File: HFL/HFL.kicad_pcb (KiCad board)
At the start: 2 copper layers, 62.6 x 37.6 mm, 28 parts, among them J1 Conn_01x06_Male, J2 FOUT, J3 PWR, J4 SHTDN, J5 HFR, K1 G5V-1, K2 G5V-1, K3 G5V-1, K4 G5V-1, K5 OMRON-G2R-24

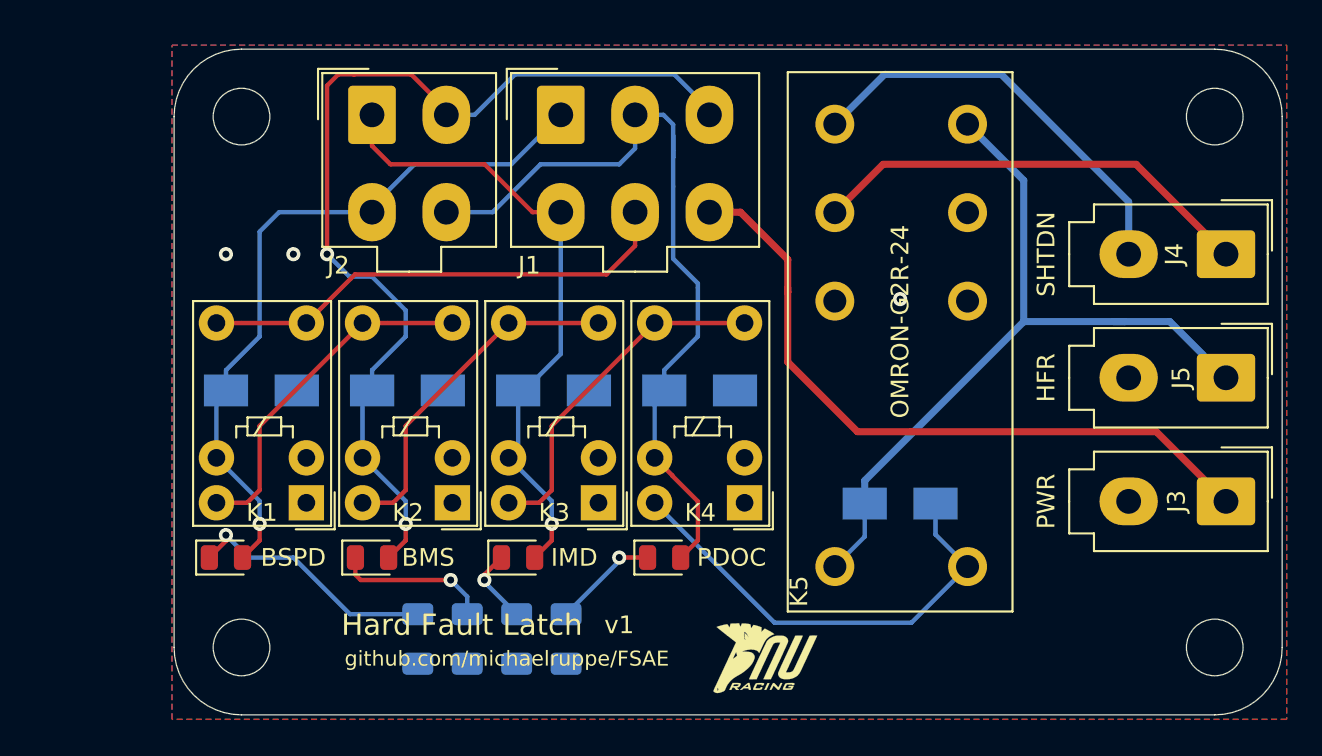
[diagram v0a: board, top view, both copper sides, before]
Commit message: Update HFL PCB - preliminary component placement
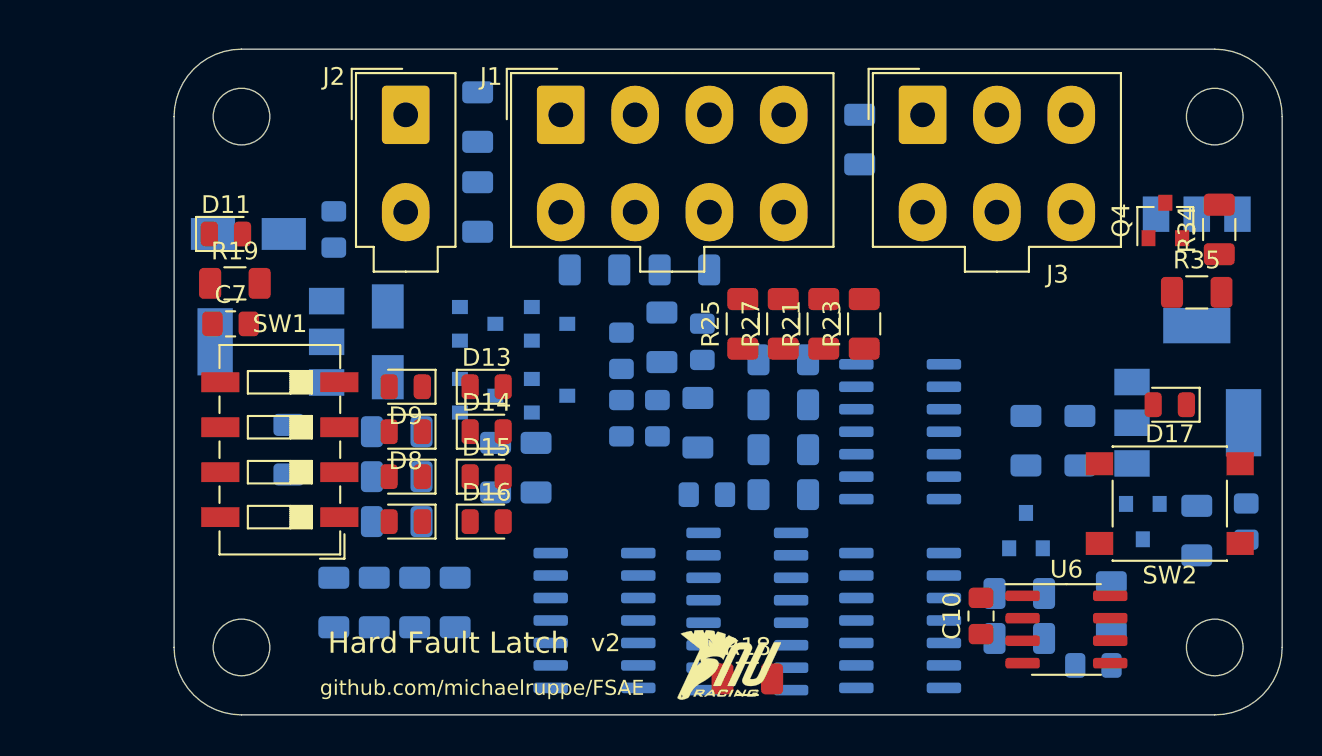
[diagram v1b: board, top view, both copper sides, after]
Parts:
- removed J4: SHTDN, Connector_Molex:Molex_Mini-Fit_Jr_5566-02A_2x01_P4.20mm_Vertical
- removed J5: HFR, Connector_Molex:Molex_Mini-Fit_Jr_5566-02A_2x01_P4.20mm_Vertical
- removed K1, K2, K3, K4: G5V-1, Relay_THT:Relay_SPDT_Omron_G5V-1
- removed K5: OMRON-G2R-24, HFL:OMRON-G2R-24
- added C1: 10n, Capacitor_SMD:C_0805_2012Metric_Pad1.15x1.40mm_HandSolder, B.Cu at (103.5, 66.6)
- added C10: 1u, Capacitor_SMD:C_0805_2012Metric_Pad1.15x1.40mm_HandSolder, F.Cu at (121.8, 77.8)
- added C2: 10n, Capacitor_SMD:C_0805_2012Metric_Pad1.15x1.40mm_HandSolder, B.Cu at (101.5, 66.6)
- added C3: 10n, Capacitor_SMD:C_0805_2012Metric_Pad1.15x1.40mm_HandSolder, B.Cu at (106.1, 62.3)
- added C4: 10n, Capacitor_SMD:C_0805_2012Metric_Pad1.15x1.40mm_HandSolder, B.Cu at (101.5, 62.8)
- added C5: 100n, Capacitor_SMD:C_0805_2012Metric_Pad1.15x1.40mm_HandSolder, B.Cu at (106.3, 70.9)
- added C6: 1u, Capacitor_SMD:C_0805_2012Metric_Pad1.15x1.40mm_HandSolder, B.Cu at (85.2, 55.9)
- added C7: 1u, Capacitor_SMD:C_0805_2012Metric_Pad1.15x1.40mm_HandSolder, F.Cu at (79.4, 61.2)
- added C8: 1u, Capacitor_SMD:C_0805_2012Metric_Pad1.15x1.40mm_HandSolder, B.Cu at (136.8, 72.4)
- added C9: 10n, Capacitor_SMD:C_0805_2012Metric_Pad1.15x1.40mm_HandSolder, B.Cu at (128.2, 80.5)
- added D10: D, Diode_SMD:D_SMA, B.Cu at (88.3, 62.3)
- added D11: PWR, LED_SMD:LED_0805_2012Metric, F.Cu at (79.1, 56.2)
- added D12: BZX84Cxx, Diode_SMD:D_SOT-23_ANK, B.Cu at (130.9, 72.4)
- added D13: IMD-OK, LED_SMD:LED_0805_2012Metric, F.Cu at (93.9, 64.8)
- added D14: BSPD-OK, LED_SMD:LED_0805_2012Metric, F.Cu at (93.9, 67.3)
- added D15: BMS-OK, LED_SMD:LED_0805_2012Metric, F.Cu at (93.9, 69.9)
- added D16: PDOC-OK, LED_SMD:LED_0805_2012Metric, F.Cu at (93.9, 72.4)
- added D17: FAULT, LED_SMD:LED_0805_2012Metric, F.Cu at (132.5, 65.8)
- added Q1: 2N7002, Package_TO_SOT_SMD:SOT-23, B.Cu at (124.3, 72.9)
- added Q2: MCT06P10-TP, Package_TO_SOT_SMD:SOT-223-3_TabPin2, B.Cu at (133.5, 66.8)
- added Q3: MCT06P10-TP, Package_TO_SOT_SMD:SOT-223-3_TabPin2, B.Cu at (134.0, 58.2)
- added Q4: 2N7002, Package_TO_SOT_SMD:SOT-23, F.Cu at (132.2, 55.4)
- added R10: 10k, Resistor_SMD:R_1206_3216Metric, B.Cu at (87.5, 77.0)
- added R11: 10k, Resistor_SMD:R_1206_3216Metric, B.Cu at (89.8, 77.0)
- added R12: 10k, Resistor_SMD:R_1206_3216Metric, B.Cu at (92.1, 77.0)
- added R13: 330, Resistor_SMD:R_1206_3216Metric, B.Cu at (88.8, 72.4)
- added R14: 330, Resistor_SMD:R_1206_3216Metric, B.Cu at (88.8, 69.9)
- added R15: 330, Resistor_SMD:R_1206_3216Metric, B.Cu at (88.8, 67.3)
- added R16: 330, Resistor_SMD:R_1206_3216Metric, B.Cu at (82.7, 68.4)
- added R17: 1k, Resistor_SMD:R_1206_3216Metric, B.Cu at (114.9, 50.8)
- added R18: 100k, Resistor_SMD:R_1206_3216Metric, F.Cu at (108.6, 81.3)
- added R19: 3k3, Resistor_SMD:R_1206_3216Metric, F.Cu at (79.6, 59.0)
- added R20: 1k, Resistor_SMD:R_1206_3216Metric, B.Cu at (134.0, 72.9)
- added R21: 1k, Resistor_SMD:R_1206_3216Metric, F.Cu at (112.9, 61.2)
- added R22: 2k7, Resistor_SMD:R_1206_3216Metric, B.Cu at (110.6, 63.3)
- added R23: 1k, Resistor_SMD:R_1206_3216Metric, F.Cu at (115.2, 61.2)
- added R24: 2k7, Resistor_SMD:R_1206_3216Metric, B.Cu at (110.6, 70.9)
- added R25: 1k, Resistor_SMD:R_1206_3216Metric, F.Cu at (108.3, 61.2)
- added R26: 2k7, Resistor_SMD:R_1206_3216Metric, B.Cu at (110.6, 68.4)
- added R27: 1k, Resistor_SMD:R_1206_3216Metric, F.Cu at (110.6, 61.2)
- added R28: 2k7, Resistor_SMD:R_1206_3216Metric, B.Cu at (110.6, 65.8)
- added R29: 100k, Resistor_SMD:R_1206_3216Metric, B.Cu at (124.0, 76.5)
- added R30: 100k, Resistor_SMD:R_1206_3216Metric, B.Cu at (124.3, 67.8)
- added R31: 10k, Resistor_SMD:R_1206_3216Metric, B.Cu at (127.4, 67.8)
- added R32: 150k, Resistor_SMD:R_1206_3216Metric, B.Cu at (124.0, 79.0)
- added R33: 100k, Resistor_SMD:R_1206_3216Metric, B.Cu at (129.2, 77.2)
- added R34: 10k, Resistor_SMD:R_1206_3216Metric, F.Cu at (135.3, 55.9)
- added R35: 2k2, Resistor_SMD:R_1206_3216Metric, F.Cu at (134.0, 59.5)
- added R5: 100k, Resistor_SMD:R_1206_3216Metric, B.Cu at (105.8, 66.8)
- added R6: 100k, Resistor_SMD:R_1206_3216Metric, B.Cu at (96.7, 69.4)
- added R7: 100k, Resistor_SMD:R_1206_3216Metric, B.Cu at (94.4, 69.4)
- added R8: 100k, Resistor_SMD:R_1206_3216Metric, B.Cu at (103.8, 62.0)
- added R9: 10k, Resistor_SMD:R_1206_3216Metric, B.Cu at (85.2, 77.0)
- added SW1: BYPASS, Button_Switch_SMD:SW_DIP_SPSTx04_Slide_6.7x11.72mm_W6.73mm_P2.54mm_LowProfile_JPin, F.Cu at (82.2, 68.4)
- added SW2: SW_Push, Button_Switch_SMD:SW_Push_1P1T_NO_6x6mm_H9.5mm, F.Cu at (132.5, 71.4)
- added U1: 74LS32, Package_SO:SOIC-14_3.9x8.7mm_P1.27mm, B.Cu at (100.0, 78.0)
- added U2: 74LS08, Package_SO:SOIC-14_3.9x8.7mm_P1.27mm, B.Cu at (117.2, 78.0)
- added U3: MCP6004, Package_SO:SOIC-14_3.9x8.7mm_P1.27mm, B.Cu at (117.2, 67.3)
- added U4: LM1117-5.0, Package_TO_SOT_SMD:SOT-223-3_TabPin2, B.Cu at (81.7, 62.3)
- added U5: 4044, Package_SO:SOIC-16_3.9x9.9mm_P1.27mm, B.Cu at (108.6, 77.5)
- added U6: NE555, Package_SO:SOIC-8_3.9x4.9mm_P1.27mm, F.Cu at (126.6, 78.5)
- D1: value BSPD-OK -> BZX84Cxx; footprint LED_SMD:LED_0805_2012Metric -> Diode_SMD:D_SOT-23_ANK; moved to B.Cu
- D2, D4: value D -> BZX84Cxx; footprint Diode_SMD:D_SMA -> Diode_SMD:D_SOT-23_ANK
- D3: value BMS-OK -> BZX84Cxx; footprint LED_SMD:LED_0805_2012Metric -> Diode_SMD:D_SOT-23_ANK; moved to B.Cu
- D5: value IMD-OK -> MAN
- D7: value PDOC-OK -> MAN
- D8, D9: value D -> MAN; footprint Diode_SMD:D_SMA -> LED_SMD:LED_0805_2012Metric; moved to F.Cu
- J1: value Conn_01x06_Male -> STS_IO; footprint Connector_Molex:Molex_Mini-Fit_Jr_5566-06A_2x03_P4.20mm_Vertical -> Connector_Molex:Molex_Mini-Fit_Jr_5566-08A_2x04_P4.20mm_Vertical
- J2: value FOUT -> PWR; footprint Connector_Molex:Molex_Mini-Fit_Jr_5566-04A_2x02_P4.20mm_Vertical -> Connector_Molex:Molex_Mini-Fit_Jr_5566-02A_2x01_P4.20mm_Vertical
- J3: value PWR -> Conn_01x06_Male; footprint Connector_Molex:Molex_Mini-Fit_Jr_5566-02A_2x01_P4.20mm_Vertical -> Connector_Molex:Molex_Mini-Fit_Jr_5566-06A_2x03_P4.20mm_Vertical
- R1, R2, R3, R4: value 2k7 -> 2k2
- moved R4 29.9 mm to (93.4, 49.6), turned to 90 degrees
- moved D9 28.7 mm to (89.3, 64.8)
- moved J3 27.8 mm to (118.5, 49.4), turned to 0 degrees
- moved R2 24.4 mm to (93.4, 54.6), turned to 90 degrees
- moved R1 23.1 mm to (100.0, 58.2), turned to 0 degrees
- moved R3 22.9 mm to (105.0, 58.2), turned to 180 degrees
- moved D1 20.4 mm to (97.4, 65.3)
- moved D6 19.4 mm to (80.4, 56.2), turned to 180 degrees
- moved D8 16.8 mm to (89.3, 67.3), turned to 180 degrees
- moved D3 16.6 mm to (97.4, 61.2)
- moved D7 15.3 mm to (89.3, 69.9), turned to 180 degrees
- moved D2 12.8 mm to (93.4, 61.2)
- moved D5 6.67 mm to (89.3, 72.4), turned to 180 degrees
- moved D4 3.98 mm to (93.4, 65.3)
- moved G*** 2.07 mm to (107.6, 80.5)
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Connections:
- D1 pad 1: Net-(D1-Pad1) -> Net-(C3-Pad1)
- D1 pad 2: BSPD-OK -> GND
- D2 pad 1: BSPD-OK -> Net-(C4-Pad1)
- D3 pad 1: Net-(D3-Pad1) -> Net-(C1-Pad1)
- D3 pad 2: BMS-OK -> GND
- D4 pad 1: BMS-OK -> Net-(C2-Pad1)
- D5 pad 2: IMD-OK -> Net-(D5-Pad2)
- D6 pad 1: IMD-OK -> +12V
- D6 pad 2: GND -> Net-(D6-Pad2)
- D7 pad 2: PDOC-OK -> Net-(D7-Pad2)
- D8 pad 1: PDOC-OK -> Net-(D8-Pad1)
- D8 pad 2: GND -> Net-(D8-Pad2)
- D9 pad 2: /HFR1 -> Net-(D9-Pad2)
- J1 pad 1: BSPD-OK -> /IMD-OKHS
- J1 pad 2: PDOC-OK -> /BMS-OKHS
- J1 pad 3: BMS-OK -> /IMD-OUT
- J1 pad 4: IMD-OK -> /BMS-OUT
- J1 pad 5: /BOTS-OK -> /BSPD-OKHS
- J1 pad 6: +12V -> /PDOC-OKHS
- J2 pad 1: IMD-OK -> Net-(D6-Pad2)
- J2 pad 2: BMS-OK -> GND
- J3 pad 1: +12V -> HFR1
- J3 pad 2: GND -> +12V
- R1 pad 1: Net-(D1-Pad1) -> Net-(C1-Pad1)
- R1 pad 2: GND -> /PDOC-OKHS
- R2 pad 1: Net-(D3-Pad1) -> Net-(C2-Pad1)
- R2 pad 2: GND -> /BSPD-OKHS
- R3 pad 1: Net-(D5-Pad1) -> Net-(C3-Pad1)
- R3 pad 2: GND -> /BMS-OKHS
- R4 pad 1: Net-(D7-Pad1) -> Net-(C4-Pad1)
- R4 pad 2: GND -> /IMD-OKHS
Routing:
- net BMS-OK: track 57.0 -> 0.00 mm, vias 2 -> 0
- net PDOC-OK: track 45.5 -> 0.00 mm
- net /HFR1: track 44.1 -> 0.00 mm
- net BSPD-OK: track 41.1 -> 0.00 mm, vias 1 -> 0
- net +12V: track 39.6 -> 0.00 mm
- net IMD-OK: track 36.3 -> 0.00 mm, vias 1 -> 0
- net /BOTS-OK: track 27.4 -> 0.00 mm
- net Net-(D9-Pad1): track 26.1 -> 0.00 mm
- net Net-(J4-Pad1): track 25.3 -> 0.00 mm
- net Net-(J4-Pad2): track 23.7 -> 0.00 mm
- net Net-(K1-Pad10): track 19.7 -> 0.00 mm
- net Net-(K3-Pad10): track 19.7 -> 0.00 mm
- net Net-(K2-Pad10): track 19.7 -> 0.00 mm
- net Net-(D1-Pad1): track 14.4 -> 0.00 mm, vias 1 -> 0
- net Net-(D3-Pad1): track 8.79 -> 0.00 mm, vias 1 -> 0
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- removed copper zone on B.Cu, net GND
- removed copper zone on F.Cu, net GND
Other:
- board text added: "v2"
- board text removed: "BMS"
- board text removed: "BSPD"
- board text removed: "HFR"
- board text removed: "IMD"
- board text removed: "PDOC"
- board text removed: "PWR"
- board text removed: "SHTDN"
- board text removed: "v1"

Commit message: Update HFL PCB Faults and statuses now independent. Working on part placement
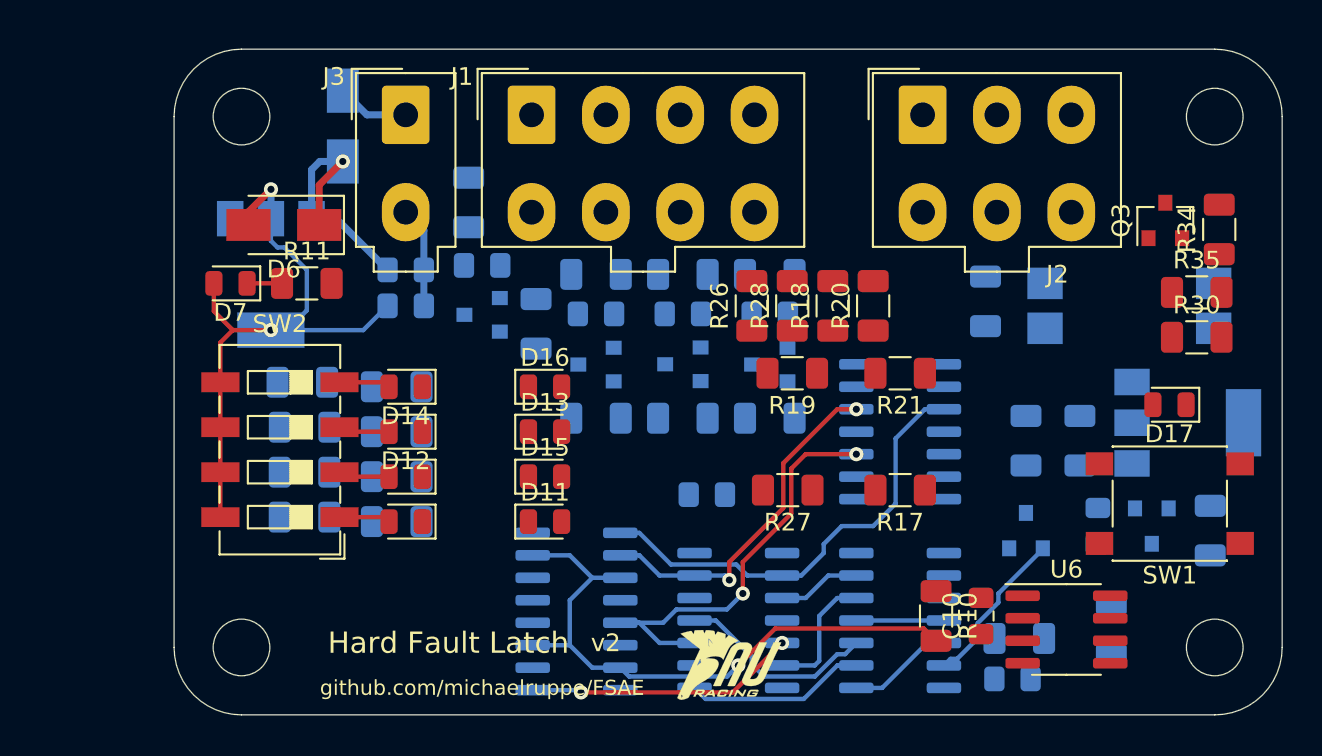
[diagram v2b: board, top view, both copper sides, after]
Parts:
- removed the Q3 at (134.0, 58.2)
- removed the R22 at (110.6, 63.3)
- removed the R26 at (110.6, 68.4)
- removed the R29 at (124.0, 76.5)
- added R17: 2k7, Resistor_SMD:R_1206_3216Metric, F.Cu at (117.2, 70.6)
- added R21: 2k7, Resistor_SMD:R_1206_3216Metric, F.Cu at (117.2, 64.0)
- added R30: 1k, Resistor_SMD:R_1206_3216Metric, F.Cu at (134.0, 62.0)
- added U7: LTV-817S, Package_DIP:SMDIP-4_W9.53mm, B.Cu at (130.2, 60.2)
- C7: moved to B.Cu
- D6: renamed from D10; moved to F.Cu
- R19: renamed from R24; moved to F.Cu
- R27: renamed from R28; moved to F.Cu
- R33: renamed from R31; value 10k -> 100k
- SW1: renamed from SW2; value SW_Push -> RST
- moved R13 15.1 mm to (83.4, 64.5), turned to 0 degrees
- moved D3 12.7 mm to (109.9, 63.5), turned to 180 degrees
- moved R14 11.7 mm to (83.6, 67.1), turned to 0 degrees
- moved C2 11.7 mm to (93.6, 57.9), turned to 0 degrees
- moved R9 11.6 mm to (122.1, 60.0)
- moved R10 11.2 mm to (119.3, 77.8), turned to 270 degrees
- moved R4 11.1 mm to (100.0, 58.4), turned to 0 degrees
- moved R7 10.9 mm to (105.0, 66.6), turned to 0 degrees
- moved C7 9.95 mm to (89.3, 60.2)
- moved R1 9.91 mm to (109.9, 58.4), turned to 180 degrees
- moved U5 9.65 mm to (98.9, 77.5), turned to 0 degrees
- moved D6 8.84 mm to (82.4, 55.7), turned to 180 degrees
- moved C1 8.66 mm to (109.9, 60.7), turned to 0 degrees
- moved C8 8.39 mm to (128.4, 72.7)
- moved R15 8.35 mm to (83.6, 69.6), turned to 0 degrees
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- renumbered D7 to D10, D13 to D11, D8 to D12, D14 to D13, D9 to D14, D6 to D5, D11 to D7, D12 to D8, D5 to D9, J3 to J2, J2 to J3, Q4 to Q3, R18 to R10, R19 to R11, R20 to R12, R12 to R13, R11 to R14, R10 to R15, R9 to R16, R21 to R18, R23 to R20, R16 to R22, R15 to R23, R14 to R24, R13 to R25, R25 to R26, R27 to R28, R30 to R29, R32 to R31, R33 to R32, R17 to R9, SW1 to SW2
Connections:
- C9 pad 1: Net-(C9-Pad1) -> Net-(C10-Pad1)
- D10 pad 2: Net-(D7-Pad2) -> /BMS-BPS
- D12 pad 2: Net-(D8-Pad2) -> /BSPD-BPS
- D14 pad 2: Net-(D9-Pad2) -> /PDOC-BPS
- D9 pad 2: Net-(D5-Pad2) (its old number) -> /IMD-BPS
- Q1 pad 3: Net-(Q1-Pad3) -> Net-(C10-Pad1)
- Q2 pad 1: Net-(Q1-Pad3) -> Net-(Q2-Pad1)
- Q2 pad 2: Net-(Q2-Pad2) -> SHTDN_IN
- R13 pad 2: Net-(D9-Pad2) -> /PDOC-BPS
- R14 pad 2: Net-(D8-Pad2) -> /BSPD-BPS
- R15 pad 2: Net-(D7-Pad2) -> /BMS-BPS
- R16 pad 2: Net-(D5-Pad2) (its old number) -> /IMD-BPS
- R18 pad 1: Net-(R21-Pad1) -> Net-(R17-Pad1)
- R19 pad 1: Net-(R23-Pad1) -> Net-(R19-Pad1)
- R20 pad 1: Net-(R23-Pad1) -> Net-(R19-Pad1)
- R26 pad 1: Net-(R25-Pad1) -> Net-(R21-Pad1)
- R29 pad 2: Net-(Q1-Pad3) -> Net-(C10-Pad1)
- R33 pad 1: Net-(Q2-Pad2) -> SHTDN_IN
- R33 pad 2: Net-(Q1-Pad3) -> Net-(Q2-Pad1)
- SW2 pad 1: Net-(D5-Pad2) (its old number) -> /IMD-BPS
- SW2 pad 2: Net-(D7-Pad2) -> /BMS-BPS
- SW2 pad 3: Net-(D8-Pad2) -> /BSPD-BPS
- SW2 pad 4: Net-(D9-Pad2) -> /PDOC-BPS
- U1 pad 1: Net-(D5-Pad2) (its old number) -> /BSPD-BPS
- U1 pad 10: Net-(C3-Pad1) -> /PDOC-OK
- U1 pad 11: Net-(U1-Pad11) -> /BMS-STS
- U1 pad 12: Net-(D9-Pad2) -> /BMS-BPS
- U1 pad 13: Net-(C4-Pad1) -> /BMS-OK
- U1 pad 2: Net-(C1-Pad1) -> /BSPD-OK
- U1 pad 3: Net-(U1-Pad3) -> /BSPD-STS
- U1 pad 4: Net-(D7-Pad2) -> /IMD-BPS
- U1 pad 5: Net-(C2-Pad1) -> /IMD-OK
- U1 pad 6: Net-(U1-Pad6) -> /IMD-STS
- U1 pad 8: Net-(U1-Pad8) -> /PDOC-STS
- U1 pad 9: Net-(D8-Pad2) -> /PDOC-BPS
- U2 pad 1: /PDOC-OK -> GND
- U2 pad 10: /IMD-OK -> /BMS-STS
- U2 pad 11: (no net) -> Net-(U2-Pad11)
- U2 pad 12: GND -> /IMD-STS
- U2 pad 13: GND -> /BSPD-STS
- U2 pad 2: /BSPD-OK -> GND
- U2 pad 3: Net-(U2-Pad3) -> (no net)
- U2 pad 4: Net-(U2-Pad3) -> Net-(U2-Pad11)
- U2 pad 9: /BMS-OK -> /PDOC-STS
- U3 pad 10: /BSPD-OK -> /PDOC-OK
- U3 pad 12: /PDOC-OK -> /BMS-OK
- U3 pad 13: Net-(R27-Pad1) -> Net-(R19-Pad1)
- U3 pad 14: Net-(R27-Pad1) -> Net-(R19-Pad1)
- U3 pad 3: /IMD-OK -> /BSPD-OK
- U3 pad 5: /BMS-OK -> /IMD-OK
- U3 pad 6: Net-(R23-Pad1) -> Net-(R17-Pad1)
- U3 pad 7: Net-(R23-Pad1) -> Net-(R17-Pad1)
- U3 pad 8: Net-(R25-Pad1) -> Net-(R27-Pad1)
- U3 pad 9: Net-(R25-Pad1) -> Net-(R27-Pad1)
- U5 pad 12: Net-(U1-Pad8) -> Net-(C3-Pad1)
- U5 pad 14: Net-(U1-Pad11) -> Net-(C4-Pad1)
- U5 pad 4: Net-(U1-Pad3) -> Net-(C1-Pad1)
- U5 pad 6: Net-(U1-Pad6) -> Net-(C2-Pad1)
- U6 pad 4: Net-(Q1-Pad3) -> Net-(C10-Pad1)
- U6 pad 5: Net-(C9-Pad1) -> Net-(C10-Pad1)
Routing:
- net +5V: track 0.00 -> 36.2 mm, vias 0 -> 2
- net Net-(C8-Pad2): track 0.00 -> 34.8 mm, vias 0 -> 1
- net /BSPD-OK: track 0.00 -> 25.6 mm
- net /PDOC-OK: track 0.00 -> 24.5 mm, vias 0 -> 2
- net /BMS-OK: track 0.00 -> 20.0 mm, vias 0 -> 2
- net /IMD-OK: track 0.00 -> 15.3 mm, vias 0 -> 2
- net +12V: track 0.00 -> 14.4 mm, vias 0 -> 1
- net /BMS-STS: track 0.00 -> 11.5 mm
- net /PDOC-STS: track 0.00 -> 10.2 mm
- net Net-(Q1-Pad1): track 0.00 -> 9.15 mm
- net /IMD-STS: track 0.00 -> 7.26 mm
- net Net-(U2-Pad5): track 0.00 -> 6.00 mm
- net GND: track 0.00 -> 5.72 mm
- net Net-(U2-Pad11): track 0.00 -> 4.95 mm
- net /BSPD-STS: track 0.00 -> 4.72 mm
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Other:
- board text added: "ToDo: Update Molex footprints"

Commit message: Update HFL - tentatively complete v2 routing still need to select parts
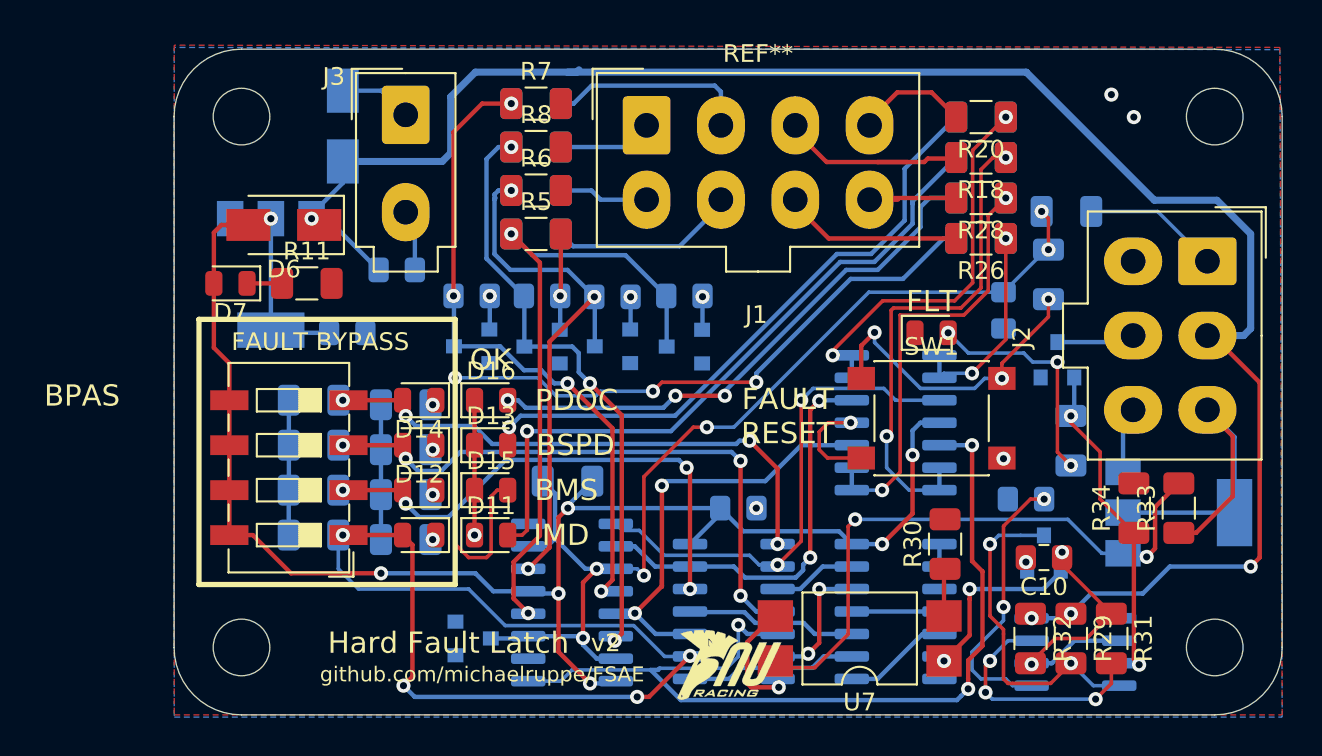
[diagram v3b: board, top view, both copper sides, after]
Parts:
- J1: footprint Connector_Molex:Molex_Mini-Fit_Jr_5566-08A_2x04_P4.20mm_Vertical -> Mini-Fit-Jr-4.20mm-pitch:Molex-Mini-Fit-Jr-8-pin-P4.2mm-RowP4.2mm
- J2: footprint Connector_Molex:Molex_Mini-Fit_Jr_5566-06A_2x03_P4.20mm_Vertical -> Mini-Fit-Jr-4.20mm-pitch:Molex-Mini-Fit-Jr-6-pin-P4.2mm-RowP4.2mm
- Q3, R10, R17, R19, R21, R27, R35, U6: moved to B.Cu
- R29, R31, R32, R33, R5, R6, R7, R8, U7: moved to F.Cu
- moved D8 38.9 mm to (93.1, 79.0), turned to 0 degrees
- moved U7 24.2 mm to (114.9, 79.0)
- moved R10 22.2 mm to (98.4, 70.1), turned to 180 degrees
- moved R27 19.8 mm to (121.8, 54.1)
- moved R7 19.6 mm to (96.7, 48.8)
- moved R17 19.3 mm to (121.8, 51.8)
- moved R30 18.4 mm to (119.8, 73.7), turned to 90 degrees
- moved R19 18.0 mm to (121.8, 49.6)
- moved R12 17.1 mm to (125.6, 58.4), turned to 270 degrees
- moved R5 16.8 mm to (96.7, 56.2)
- moved J1 16.7 mm to (109.1, 60.2)
- moved R34 16.5 mm to (130.4, 71.7)
- moved R8 15.7 mm to (96.7, 51.3)
- moved SW1 14.3 mm to (119.0, 66.6), turned to 0 degrees
- moved D17 14.0 mm to (119.0, 61.8), turned to 0 degrees
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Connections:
- C9 pad 1: Net-(C10-Pad1) -> Net-(C9-Pad1)
- Q1 pad 3: Net-(C10-Pad1) -> Net-(Q1-Pad3)
- R13 pad 2: /PDOC-BPS -> /IMD-BPS
- R14 pad 2: /BSPD-BPS -> /PDOC-BPS
- R16 pad 2: /IMD-BPS -> /BSPD-BPS
- R29 pad 2: Net-(C10-Pad1) -> Net-(Q1-Pad3)
- U1 pad 1: /BSPD-BPS -> /PDOC-BPS
- U1 pad 4: /IMD-BPS -> /BSPD-BPS
- U1 pad 9: /PDOC-BPS -> /IMD-BPS
- U6 pad 4: Net-(C10-Pad1) -> Net-(Q1-Pad3)
- U6 pad 5: Net-(C10-Pad1) -> Net-(C9-Pad1)
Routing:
- net +12V: track 14.4 -> 105.0 mm, vias 1 -> 4
- net +5V: track 36.2 -> 95.3 mm, vias 2 -> 7
- net /IMD-BPS: track 2.91 -> 53.3 mm, vias 0 -> 4
- net Net-(D15-Pad2): track 0.00 -> 48.9 mm, vias 0 -> 3
- net GND: track 5.72 -> 51.2 mm, vias 0 -> 12
- net Net-(D11-Pad2): track 0.00 -> 38.5 mm, vias 0 -> 1
- net /IMD-OK: track 15.3 -> 51.8 mm, vias 2 -> 3
- net Net-(C3-Pad1): track 0.00 -> 36.4 mm, vias 0 -> 4
- net Net-(C1-Pad1): track 0.00 -> 36.1 mm, vias 0 -> 2
- net Net-(D13-Pad2): track 0.00 -> 35.3 mm, vias 0 -> 1
- net Net-(C4-Pad1): track 0.00 -> 34.1 mm, vias 0 -> 3
- net Net-(Q2-Pad1): track 0.00 -> 34.0 mm, vias 0 -> 2
- net Net-(D16-Pad2): track 0.00 -> 31.2 mm, vias 0 -> 3
- net /BSPD-BPS: track 2.91 -> 33.8 mm, vias 0 -> 4
- net Net-(C2-Pad1): track 0.00 -> 30.9 mm, vias 0 -> 3
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- added copper zone on B.Cu, net GND
- added copper zone on F.Cu, net GND
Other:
- board text added: "BMS"
- board text added: "BPAS"
- board text added: "BSPD"
- board text added: "FAULT BYPASS"
- board text added: "FAULT RESET"
- board text added: "FLT"
- board text added: "IMD"
- board text added: "OK"
- board text added: "PDOC"
- board text removed: "ToDo: Update Molex footprints"
